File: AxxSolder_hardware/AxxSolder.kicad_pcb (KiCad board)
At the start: 2 copper layers, 39 x 71 mm, 91 parts, among them IC1 LTC4440AHMS8E-5#PBF, IC2 STM32G431KBT6, IC3 TMP236AQDBZRQ1, IC4 OPA2333AIDRBR, IC5 STM32G431KBT6, IC6 TPS54302DDCR, J1 Conn_01x07_Male, J4 Conn_01x07_Male, Q2 2N7002NXAKR, U1 PEC11L-4220F-S0015, U2 BSC014N04LS

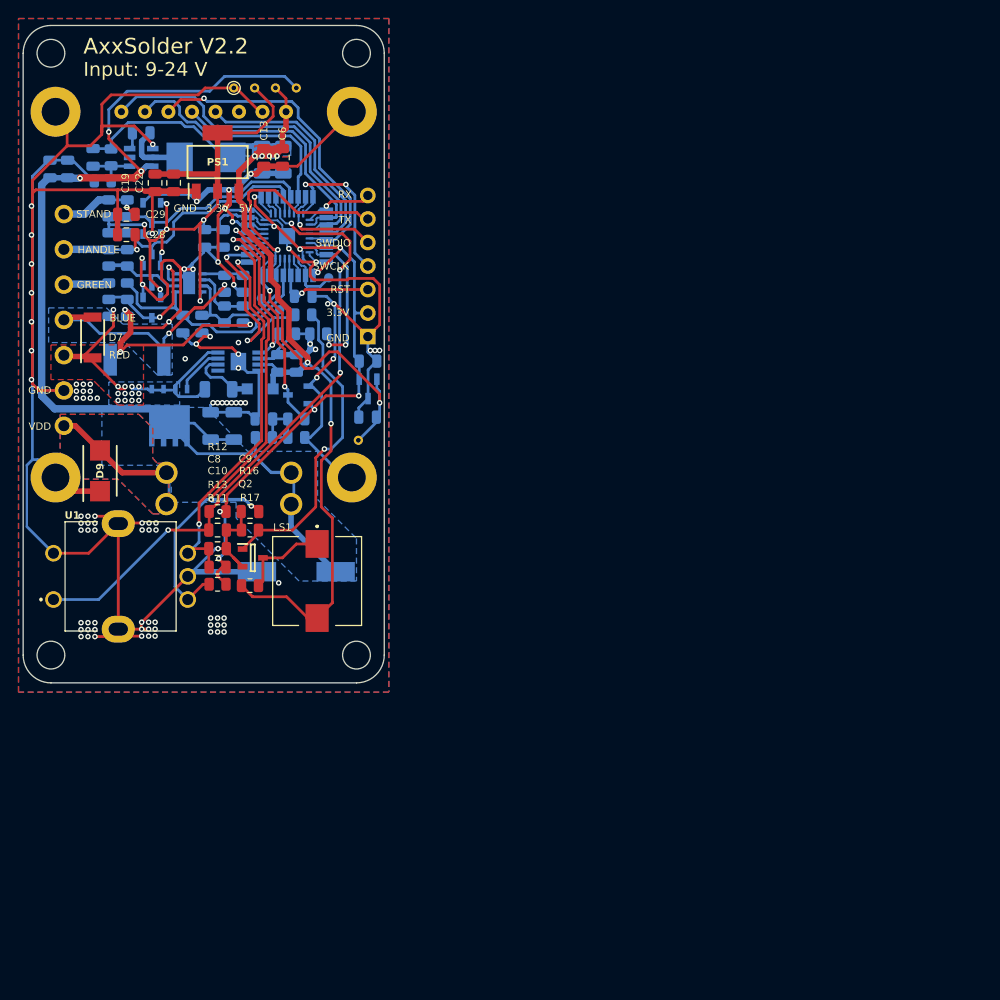
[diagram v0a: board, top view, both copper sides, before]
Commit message: update USBC-PD branch
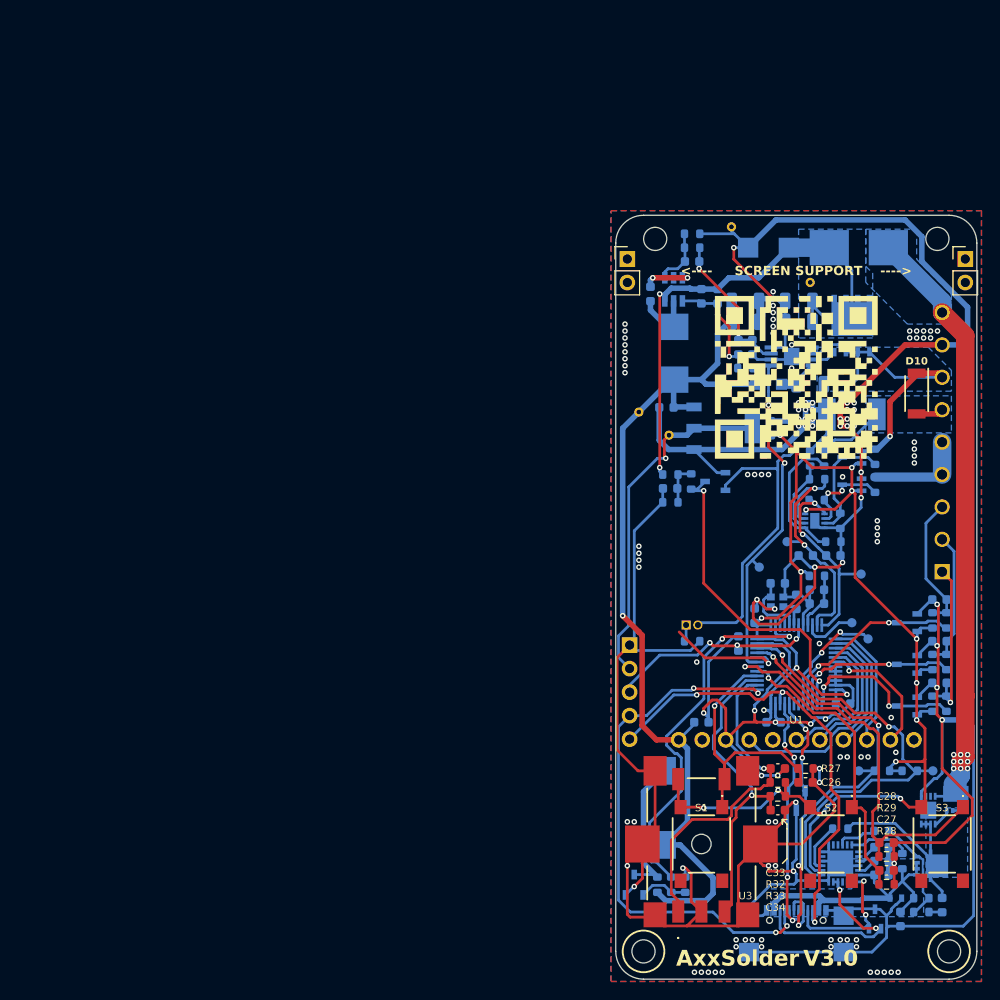
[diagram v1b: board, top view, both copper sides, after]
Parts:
- removed C23: 330u, EMZR500ARA331MJA0G:CAPAE1030X1050N
- removed the D5 at (110.9, 74.0)
- removed H3, H4: MountingHole, MountingHole:MountingHole_3mm
- removed the IC5 at (125.5, 69.8)
- removed the R16 at (121.5, 101.5)
- removed the R17 at (121.5, 107.5)
- removed the R22 at (108.2, 73.9)
- removed the R26 at (120.8, 78.2)
- removed TP3: GND_TP, TestPoint:TestPoint_THTPad_D1.0mm_Drill0.5mm
- removed U2: BSC014N04LS, BSC014N04LS:BSC014N04LS
- added C1: 100n, Capacitor_SMD:C_0603_1608Metric, B.Cu at (166.5, 88.2)
- added C17: 1u, Capacitor_SMD:C_0603_1608Metric, B.Cu at (189.7, 137.2)
- added C18: 1u, Capacitor_SMD:C_0603_1608Metric, B.Cu at (189.7, 135.8)
- added C19: 10u, Capacitor_SMD:C_0603_1608Metric, B.Cu at (191.8, 143.5)
- added C28: 100n, Capacitor_SMD:C_0603_1608Metric, F.Cu at (190.2, 135.2)
- added C29: 100n, Capacitor_SMD:C_0603_1608Metric, B.Cu at (166.9, 97.0)
- added C32: 100n, Capacitor_SMD:C_0603_1608Metric, B.Cu at (196.0, 109.0)
- added C33: 100n, Capacitor_SMD:C_0603_1608Metric, F.Cu at (178.5, 127.2)
- added C34: 100n, Capacitor_SMD:C_0603_1608Metric, F.Cu at (178.5, 131.7)
- added C4: 100n, Capacitor_SMD:C_0603_1608Metric, B.Cu at (164.8, 76.0)
- added D1: BAV199WQ-7, footprints:SOT65P210X110-3N, B.Cu at (186.5, 93.7)
- added D10: PMEG10030ELPX, footprints:SODFL4725X110N, F.Cu at (193.5, 86.8)
- added D11: ESDA25P35, footprints:ESDA25P351U1M, B.Cu at (191.2, 141.2)
- added D3: ESDA25W, footprints:SOT65P210X110-3N, B.Cu at (189.0, 143.5)
- added FB1: BLM18HE601SN1D, Resistor_SMD:R_0603_1608Metric, B.Cu at (182.7, 106.4)
- added G***: LOGO, LOGO, F.Cu at (180.5, 85.0)
- added IC1: OPA2387DSGT, footprints:SON50P200X200X80-9N, B.Cu at (182.5, 100.5)
- added J2: 691243110009, footprints:691243110009, B.Cu at (196.2, 106.0)
- added J3: Conn_01x05_Socket, Connector_PinSocket_2.54mm:PinSocket_1x05_P2.54mm_Vertical, B.Cu at (162.5, 113.9)
- added Q1: STL9P3LLH6, footprints:STL20N6F7, B.Cu at (195.0, 137.8)
- added Q3: STL10N3LLH5, footprints:STL10N3LLH5, B.Cu at (197.7, 130.4)
- added R15: 1k, Resistor_SMD:R_0603_1608Metric, B.Cu at (185.2, 133.8)
- added R18: 4k7, Resistor_SMD:R_0603_1608Metric, B.Cu at (195.2, 111.2)
- added R27: 4k7, Resistor_SMD:R_0603_1608Metric, F.Cu at (181.5, 127.2)
- added R30: 6k8, Resistor_SMD:R_0603_1608Metric, B.Cu at (166.9, 98.5)
- added R32: 4k7, Resistor_SMD:R_0603_1608Metric, F.Cu at (178.5, 128.8)
- added R33: 4k7, Resistor_SMD:R_0603_1608Metric, F.Cu at (178.5, 130.2)
- added R34: 4k7, Resistor_SMD:R_0603_1608Metric, B.Cu at (168.5, 139.8)
- added R39: 5m, footprints:RESC6432X89N, B.Cu at (186.5, 89.0)
- added R4: 4k7, Resistor_SMD:R_0603_1608Metric, B.Cu at (183.5, 93.8)
- added R40: 4k7, Resistor_SMD:R_0603_1608Metric, B.Cu at (169.2, 113.5)
- added R5: 1k5, Resistor_SMD:R_0603_1608Metric, B.Cu at (189.0, 96.6)
- added R6: 100k, Resistor_SMD:R_0603_1608Metric, B.Cu at (169.2, 71.0)
- added R7: 4k7, Resistor_SMD:R_0603_1608Metric, B.Cu at (182.0, 93.8)
- added R8: 360k, Resistor_SMD:R_0603_1608Metric, B.Cu at (182.7, 98.2)
- added R9: 220k, Resistor_SMD:R_0603_1608Metric, B.Cu at (182.8, 96.0)
- added REF**: PinHeader_1x02_P2.54mm_Vertical, Connector_PinHeader_2.54mm:PinHeader_1x02_P2.54mm_Vertical, F.Cu at (162.2, 72.2)
- added REF**: PinHeader_1x02_P2.54mm_Vertical, Connector_PinHeader_2.54mm:PinHeader_1x02_P2.54mm_Vertical, F.Cu at (198.8, 72.2)
- added S1: ADTSM644KVTR, footprints:ADTSM644KVTR, F.Cu at (170.2, 135.4)
- added S2: ADTSM644KVTR, footprints:ADTSM644KVTR, F.Cu at (184.2, 135.4)
- added S3: ADTSM644KVTR, footprints:ADTSM644KVTR, F.Cu at (196.2, 135.4)
- added TP10: DIAG_TP, TestPoint:TestPoint_Pad_D1.0mm, B.Cu at (188.2, 113.2)
- added TP11: DIAG_TP, TestPoint:TestPoint_Pad_D1.0mm, B.Cu at (187.2, 127.5)
- added TP12: DIAG_TP, TestPoint:TestPoint_Pad_D1.0mm, B.Cu at (195.2, 127.5)
- added TP4: Current_TP, TestPoint:TestPoint_Pad_D1.0mm, B.Cu at (179.5, 102.8)
- added U3: PEC11J-9220F-S0015, footprints:PEC11J9220FS0015, F.Cu at (170.2, 135.4)
- added U4: BSC014N04LS, footprints:BSC014N04LS, B.Cu at (186.5, 76.3)
- added Y1: NX2016SA-32M-EXS00A-CS06465, footprints:NX2016SA32MEXS00ACS06465, B.Cu at (178.4, 109.2)
- C10: value 100n -> 1n; footprint Capacitor_SMD:C_0805_2012Metric -> Capacitor_SMD:C_0603_1608Metric; moved to B.Cu
- C11: value 100n -> 1n; footprint Capacitor_SMD:C_0805_2012Metric -> Capacitor_SMD:C_0603_1608Metric
- C12: value 10u -> 10p; footprint Capacitor_SMD:C_0805_2012Metric -> Capacitor_SMD:C_0603_1608Metric
- C13, C22, C6: footprint Capacitor_SMD:C_0805_2012Metric -> Capacitor_SMD:C_0603_1608Metric; moved to B.Cu
- C14: value 10u -> 100n; footprint Capacitor_SMD:C_0805_2012Metric -> Capacitor_SMD:C_0603_1608Metric
- C15: value 1n -> 10u; footprint Capacitor_SMD:C_0805_2012Metric -> Capacitor_SMD:C_0603_1608Metric
- C16: value 1n -> 1u; footprint Capacitor_SMD:C_0805_2012Metric -> Capacitor_SMD:C_0603_1608Metric
- C2: renamed from C19; footprint Capacitor_SMD:C_0805_2012Metric -> Capacitor_SMD:C_0603_1608Metric; moved to B.Cu
- C20, C21, C24, C5: footprint Capacitor_SMD:C_0805_2012Metric -> Capacitor_SMD:C_0603_1608Metric
- C25: value 22u -> 10u; footprint Capacitor_SMD:C_1206_3216Metric -> Capacitor_SMD:C_0603_1608Metric
- C26: value 75p -> 100n; footprint Capacitor_SMD:C_0805_2012Metric -> Capacitor_SMD:C_0603_1608Metric; moved to F.Cu
- C27: value 22u -> 100n; footprint Capacitor_SMD:C_1206_3216Metric -> Capacitor_SMD:C_0603_1608Metric; moved to F.Cu
- C3: value 100n -> 10p; footprint Capacitor_SMD:C_0805_2012Metric -> Capacitor_SMD:C_0603_1608Metric
- C30: renamed from C29; footprint Capacitor_SMD:C_0805_2012Metric -> Capacitor_SMD:C_0603_1608Metric; moved to B.Cu
- C31: renamed from C28; footprint Capacitor_SMD:C_0805_2012Metric -> Capacitor_SMD:C_0603_1608Metric; moved to B.Cu
- C36: renamed from C1; footprint Capacitor_SMD:C_0805_2012Metric -> Capacitor_SMD:C_0603_1608Metric
- C37: renamed from C2; footprint Capacitor_SMD:C_0805_2012Metric -> Capacitor_SMD:C_0603_1608Metric
- C7: value 100n -> 75p; footprint Capacitor_SMD:C_0805_2012Metric -> Capacitor_SMD:C_0603_1608Metric
- C8, C9: value 100n -> 22u; footprint Capacitor_SMD:C_0805_2012Metric -> Capacitor_SMD:C_1206_3216Metric; moved to B.Cu
- D12: value BAT54S -> TPD2E2U06; footprint BAT54S,215:SOT95P230X110-3N -> footprints:SOT95P237X95-3N
- D2: value PMEG6020ER -> BAV199WQ-7; footprint PMEG6020ER,115:PMEG6020ER115 -> footprints:SOT65P210X110-3N
- D4: value Waveshare 1.5inch OLED Module -> SMBJ24A; footprint 1_5inch-rgb-oled-module_asm-1110:1_5inch-rgb-oled-module_asm-1110 -> footprints:DIOM5436X261N; moved to B.Cu
- D5: renamed from D6; footprint BAT54S,215:SOT95P230X110-3N -> footprints:SOT95P230X110-3N
- D6: renamed from D3; footprint BAT54S,215:SOT95P230X110-3N -> footprints:SOT95P230X110-3N
- D7: value PMEG10030ELPX -> BAT54S; footprint PMEG10030ELPX:SODFL4725X110N -> footprints:SOT95P230X110-3N; moved to B.Cu
- D8: renamed from D1; footprint BAT54S,215:SOT95P230X110-3N -> footprints:SOT95P230X110-3N
- D9: value SMBJ24CA -> PMEG6020ER; footprint SMBJ24CA:DIOM5436X261N -> footprints:PMEG6020ER115; moved to B.Cu
- F1: value 10A Fuse -> 0154007.DRL; footprint 3557-2:3557-2 -> footprints:0154100DR
- H1: footprint MountingHole:MountingHole_3mm -> MountingHole:MountingHole_2.5mm; moved to F.Cu
- H2: footprint MountingHole:MountingHole_3mm -> MountingHole:MountingHole_2.5mm
- IC2: value STM32G431KBT6 -> STM32F303CCT6TR; footprint STM32G431KBT6:QFP80P900X900X160-32N -> footprints:QFP50P900X900X160-48N
- IC3: value TMP236AQDBZRQ1 -> TPS54302DDCR; footprint TMP236AQDBZRQ1:SOT95P237X112-3N -> footprints:SOT95P280X110-6N
- IC4: value OPA2333AIDRBR -> STUSB4500QTR; footprint OPA2333AIDRBR:SON65P300X300X100-9N-D -> footprints:QFN50P400X400X100-25N-D
- IC5: renamed from IC1; value LTC4440AHMS8E-5#PBF -> LTC4440AHMS8E; footprint LTC4440AHMS8E-5#PBF:SOP65P490X110-9N -> footprints:SOP65P490X110-9N
- IC6: value TPS54302DDCR -> MAX16171ATA_VY+T; footprint TPS54302DDCR:SOT95P280X110-6N -> footprints:SON50P300X200X80-9N
- J1: value Conn_01x07_Male -> USB4110-GF-A; footprint 691243310007:691243310007 -> footprints:USB4110GFA
- J4: value Conn_01x07_Male -> Conn_01x02_Pin; footprint Connector_PinSocket_2.54mm:PinSocket_1x07_P2.54mm_Vertical -> Connector_PinHeader_1.27mm:PinHeader_1x02_P1.27mm_Vertical
- L1: value SRP7028CC-100M -> SRP7028CC; footprint SRP7028CC-100M:INDPM7366X300N -> footprints:INDPM7366X300N
- LS1: footprint CMI-9653S-SMT-TR:CMI9653SSMTTR -> footprints:CMI9653SSMTTR; moved to B.Cu
- PS1: footprint LD1117AS33TR:SOT230P700X190-4N -> footprints:SOT230P700X190-4N; moved to B.Cu
- Q2: footprint 2N7002NXAKR:SOT95P230X110-3N -> footprints:SOT95P230X110-3N; moved to B.Cu
- R1: value 4k7 -> 1k5; footprint Resistor_SMD:R_0805_2012Metric -> Resistor_SMD:R_0603_1608Metric
- R10: value 2m -> 13k3; footprint WSLP25122L500FEA:RESC6432X89N -> Resistor_SMD:R_0603_1608Metric
- R11: value 10k -> 22k; footprint Resistor_SMD:R_0805_2012Metric -> Resistor_SMD:R_0603_1608Metric; moved to B.Cu
- R12: value 10k -> 100; footprint Resistor_SMD:R_0805_2012Metric -> Resistor_SMD:R_0603_1608Metric; moved to B.Cu
- R13: value 10k -> 1k; footprint Resistor_SMD:R_0805_2012Metric -> Resistor_SMD:R_0603_1608Metric; moved to B.Cu
- R14: value 10k -> 22k; footprint Resistor_SMD:R_0805_2012Metric -> Resistor_SMD:R_0603_1608Metric
- R16: renamed from R8; value 10k -> 4k7; footprint Resistor_SMD:R_0805_2012Metric -> Resistor_SMD:R_0603_1608Metric
- R17: renamed from R9; value 10k -> 4k7; footprint Resistor_SMD:R_0805_2012Metric -> Resistor_SMD:R_0603_1608Metric
- R19, R20: value 1k5 -> 4k7; footprint Resistor_SMD:R_0805_2012Metric -> Resistor_SMD:R_0603_1608Metric
- R2: value 47k -> 360k; footprint Resistor_SMD:R_0805_2012Metric -> Resistor_SMD:R_0603_1608Metric
- R21: value 470k -> 47k; footprint Resistor_SMD:R_0805_2012Metric -> Resistor_SMD:R_0603_1608Metric
- R22: renamed from R6; footprint Resistor_SMD:R_0805_2012Metric -> Resistor_SMD:R_0603_1608Metric
- R23, R24: value 220k -> 4k7; footprint Resistor_SMD:R_0805_2012Metric -> Resistor_SMD:R_0603_1608Metric
- R25: footprint Resistor_SMD:R_0805_2012Metric -> Resistor_SMD:R_0603_1608Metric
- R26: renamed from R5; footprint Resistor_SMD:R_0805_2012Metric -> Resistor_SMD:R_0603_1608Metric
- R28: value 100k -> 4k7; footprint Resistor_SMD:R_0805_2012Metric -> Resistor_SMD:R_0603_1608Metric; moved to F.Cu
- R29: value 13k3 -> 4k7; footprint Resistor_SMD:R_0805_2012Metric -> Resistor_SMD:R_0603_1608Metric; moved to F.Cu
- R3: value 6k8 -> 220k; footprint Resistor_SMD:R_0805_2012Metric -> Resistor_SMD:R_0603_1608Metric
- R31: renamed from R15; footprint Resistor_SMD:R_0805_2012Metric -> Resistor_SMD:R_0603_1608Metric
- R35: renamed from R18; value 10k -> 4k7; footprint Resistor_SMD:R_0805_2012Metric -> Resistor_SMD:R_0603_1608Metric
- TP1: value AmbTemp_TP -> VDD_TP
- TP2: value TestPoint -> 3.3V_TP; footprint TestPoint:TestPoint_Pad_D1.0mm -> TestPoint:TestPoint_THTPad_D1.0mm_Drill0.5mm
- TP5: value Thermocouple_TP -> TC_TP
- TP6: value Current_TP -> GND_TP; footprint TestPoint:TestPoint_Pad_D1.0mm -> TestPoint:TestPoint_THTPad_D1.0mm_Drill0.5mm
- TP7: value 5V_TP -> VDD_TP
- TP8: value VDD_TP -> SW_TP; footprint TestPoint:TestPoint_THTPad_D1.0mm_Drill0.5mm -> TestPoint:TestPoint_Pad_D1.0mm
- TP9: value 3.3V_TP -> DIAG_TP; footprint TestPoint:TestPoint_THTPad_D1.0mm_Drill0.5mm -> TestPoint:TestPoint_Pad_D1.0mm
- U1: value PEC11L-4220F-S0015 -> ~; footprint PEC11L-4220F-S0015:PEC11L4220FS0015 -> footprints:Adafruit_240x320_TFT
- moved R28 114.8 mm to (190.2, 139.8), turned to 0 degrees
- moved R29 111.7 mm to (190.2, 136.8), turned to 0 degrees
- moved IC6 110.4 mm to (194.8, 131.8), turned to 90 degrees
- moved C13 109.0 mm to (196.2, 142.0)
- moved J1 104.0 mm to (180.5, 146.2), turned to 180 degrees
- moved R16 103.8 mm to (195.2, 120.2)
- moved R26 103.4 mm to (196.7, 120.2)
- moved C26 102.4 mm to (181.5, 128.8), turned to 0 degrees
- moved H2 102.1 mm to (197.0, 147.0)
- moved C21 101.7 mm to (185.6, 120.2), turned to 0 degrees
- moved C30 101.3 mm to (196.0, 118.0)
- moved C27 100.7 mm to (190.2, 138.2), turned to 0 degrees
- moved R17 99.9 mm to (195.2, 115.8), turned to 90 degrees
- moved R22 99.5 mm to (196.7, 115.8), turned to 90 degrees
- moved C31 98.2 mm to (196.0, 113.5)
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- renumbered C4 to C35, C17 to C38, C18 to C39
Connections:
- C10 pad 1: /ENC_A -> /TC
- C11 pad 1: +3.3V -> /Current
- C12 pad 1: +3.3V -> GND
- C12 pad 2: GND -> Net-(IC2-PF1/OSC_OUT)
- C13 pad 1: GND -> Net-(C13-Pad1)
- C13 pad 2: +5V -> /VDD_IN_USBCPD
- C14 pad 2: VDD -> /NRST
- C15 pad 1: /Thermocouple -> GND
- C15 pad 2: GND -> +5V
- C16 pad 1: /Current -> /VBUS
- C20 pad 1: /Ambient_temp -> +3.3V
- C21 pad 1: GND -> +3.3V
- C21 pad 2: VDD -> GND
- C24 pad 1: Net-(IC6-BOOT) -> /VCCA
- C24 pad 2: Net-(IC6-SW) -> GND
- C25 pad 1: GND -> /VCCA
- C25 pad 2: +5V -> GND
- C26 pad 1: Net-(IC6-FB) -> /SW1
- C26 pad 2: +5V -> GND
- C27 pad 1: GND -> /SW2
- C27 pad 2: +5V -> GND
- C3 pad 1: Net-(C3-Pad1) -> Net-(IC2-PF0/OSC_IN)
- C31 pad 1: /Handle_sense -> /Handle_sense2
- C35 pad 2: Net-(IC1-BOOST) -> Net-(IC5-TS)
- C5 pad 1: +3.3V -> GND
- C5 pad 2: GND -> VDD
- C6 pad 2: +5V -> VDD
- C7 pad 1: GND -> Net-(IC3-FB)
- C7 pad 2: /NRST -> +5V
- C8 pad 1: /ENC_Button -> GND
- C8 pad 2: GND -> +5V
- C9 pad 1: /ENC_B -> GND
- C9 pad 2: GND -> +5V
- D12 pad 1: GND -> /USB_D+
- D12 pad 2: +3.3V -> /USB_D-
- D12 pad 3: /Busvoltage -> GND
- D2 pad 1: Net-(IC1-BOOST) -> GND
- D2 pad 2: +5V -> +3.3V
- D4 pad 1: +5V -> VDD
- D5 pad 3: Net-(D6-common) -> /Handle_inp1
- D6 pad 3: /Handle_inp -> /Handle_inp2
- D7 pad 1: /RED -> GND
- D7 pad 2: /BLUE -> +3.3V
- D9 pad 1: GND -> Net-(IC5-TS)
- D9 pad 2: Net-(J1-Pin_7) -> +5V
- F1 pad 2: Net-(J1-Pin_7) -> /VDD_IN
- IC2 pad 10: /Buzzer -> /USR1
- IC2 pad 11: /ENC_B -> /Current
- IC2 pad 12: /Heater -> /TC
- IC2 pad 13: /Busvoltage -> /SPI_DC
- IC2 pad 14: GND -> /SPI_RST
- IC2 pad 15: +3.3V -> /SPI_SCK
- IC2 pad 16: GND -> /SPI_CS
- IC2 pad 17: +3.3V -> /SPI_MOSI
- IC2 pad 18: Net-(IC2-PA8) -> /SD_CS
- IC2 pad 19: /ENC_Button -> GND
- IC2 pad 2: Net-(IC2-PF0-OSC_IN) -> /Buzzer
- IC2 pad 20: /Handle_inp -> GND
- IC2 pad 21: /Stand_inp -> GND
- IC2 pad 22: /SPI_DC -> GND
- IC2 pad 23: /SWDIO -> GND
- IC2 pad 24: /SWCLK -> +3.3V
- IC2 pad 25: /MCU_RX -> /Stand_inp
- IC2 pad 26: /SPI_SCK -> /VDD_inp
- IC2 pad 27: /SPI_RST -> /Handle_inp2
- IC2 pad 28: /SPI_MOSI -> /Handle_inp1
- IC2 pad 29: /SPI_CS -> /USR2
- IC2 pad 3: Net-(IC2-PF1-OSC_OUT) -> unconnected-(IC2-PC14/OSC32_IN-Pad3)
- IC2 pad 30: Net-(IC2-PB7) -> unconnected-(IC2-PA9-Pad30)
- IC2 pad 31: Net-(IC2-PB8-BOOT0) -> unconnected-(IC2-PA10-Pad31)
- IC2 pad 32: GND -> /USB_D-
- IC2 pad 4: /NRST -> unconnected-(IC2-PC15/OSC32_OUT-Pad4)
- IC2 pad 5: /Thermocouple -> Net-(IC2-PF0/OSC_IN)
- IC2 pad 6: /Current -> Net-(IC2-PF1/OSC_OUT)
- IC2 pad 7: /MCU_TX -> /NRST
- IC2 pad 8: /Ambient_temp -> GND
- IC2 pad 9: /ENC_A -> /VCCA
- IC3 pad 1: +3.3V -> GND
- IC3 pad 2: /Ambient_temp -> Net-(IC3-SW)
- IC3 pad 3: GND -> VDD
- IC4 pad 1: /Thermocouple -> /CC1
- IC4 pad 2: Net-(D5-common) -> /CC1
- IC4 pad 3: Net-(D6-common) -> (no net)
- IC4 pad 4: GND -> /CC2
- IC4 pad 5: Net-(IC4-+IN_B) -> /CC2
- IC4 pad 6: Net-(IC4--IN_B) -> GND
- IC4 pad 7: /Current -> /SCL
- IC4 pad 8: +3.3V -> /SDA
- IC4 pad 9: GND -> Net-(IC4-DISCH)
- IC5 pad 6: Net-(IC1-BOOST) -> /RED
- IC5 pad 8: /RED -> Net-(IC5-TS)
- IC6 pad 1: GND -> Net-(IC6-GATE)
- IC6 pad 2: Net-(IC6-SW) -> /VDD_IN_USBCPD
- IC6 pad 3: VDD -> /VDD_IN_USBCPD
- IC6 pad 4: Net-(IC6-FB) -> /VDD_IN_USBCPD
- IC6 pad 5: unconnected-(IC6-EN-Pad5) -> GND
- IC6 pad 6: Net-(IC6-BOOT) -> (no net)
- J4 pad 1: GND -> /BOOT0
- L1 pad 1: Net-(IC6-SW) -> Net-(IC3-SW)
- R1 pad 1: Net-(C3-Pad1) -> /RED
- R1 pad 2: /Busvoltage -> Net-(IC1A-+)
- R10 pad 1: /BLUE -> Net-(IC3-FB)
- R11 pad 1: /ENC_B -> Net-(Q1-G)
- R11 pad 2: +3.3V -> /VBUS
- R12 pad 1: +3.3V -> Net-(Q1-G)
- R12 pad 2: /ENC_Button -> Net-(C13-Pad1)
- R13 pad 1: +3.3V -> /VBUS
- R13 pad 2: /ENC_A -> Net-(IC4-VBUS_VS_DISCH)
- R14 pad 1: GND -> Net-(IC4-VBUS_EN_SNK)
- R14 pad 2: Net-(IC2-PB8-BOOT0) -> Net-(Q1-G)
- R17 pad 2: /Handle_sense -> /Handle_sense2
- R19 pad 1: /GREEN -> /Handle_inp1
- R19 pad 2: Net-(D5-common) -> /Handle_sense1
- R2 pad 1: VDD -> Net-(IC1A-+)
- R2 pad 2: Net-(C3-Pad1) -> GND
- R20 pad 1: /RED -> +5V
- R20 pad 2: Net-(D6-common) -> Net-(LS1--)
- R21 pad 1: Net-(D6-common) -> VDD
- R21 pad 2: GND -> Net-(C29-Pad1)
- R22 pad 1: /Handle_inp -> /Handle_inp2
- R22 pad 2: /Handle_sense -> /Handle_sense2
- R23 pad 1: Net-(IC4-+IN_B) -> /SCL
- R23 pad 2: GND -> +3.3V
- R24 pad 1: Net-(IC4--IN_B) -> /SDA
- R24 pad 2: /Current -> +3.3V
- R25 pad 1: Net-(IC4-+IN_B) -> Net-(C29-Pad1)
- R25 pad 2: /BLUE -> /VDD_inp
- R28 pad 1: +5V -> /SW2
- R28 pad 2: Net-(IC6-FB) -> GND
- R29 pad 1: Net-(IC6-FB) -> /SW3
- R3 pad 1: Net-(C3-Pad1) -> Net-(IC1B-+)
- TP1 pad 1: /Ambient_temp -> +5V
- TP2 pad 1: Net-(IC2-PF0-OSC_IN) -> +3.3V
- TP5 pad 1: /Thermocouple -> /TC
- TP6 pad 1: /Current -> GND
- TP7 pad 1: +5V -> VDD
- TP8 pad 1: VDD -> /Heater
- TP9 pad 1: +3.3V -> /USR1
- U1 pad 1: /ENC_Button -> +5V
- U1 pad 2: GND -> unconnected-(U1-NC-Pad2)
- U1 pad 3: /ENC_B -> GND
- U1 pad 4: GND -> /SPI_SCK
- U1 pad 5: /ENC_A -> unconnected-(U1-NC-Pad5)
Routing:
- net GND: track 451.4 -> 600.5 mm, vias 103 -> 132
- net +3.3V: track 153.7 -> 231.8 mm, vias 16 -> 19
- net /ENC_Button: track 69.0 -> 0.00 mm, vias 4 -> 0
- net VDD: track 122.6 -> 56.9 mm, vias 3 -> 2
- net /VDD_IN: track 0.00 -> 64.2 mm, vias 0 -> 9
- net /SDA: track 0.00 -> 46.8 mm, vias 0 -> 2
- net /SW3: track 0.00 -> 43.2 mm, vias 0 -> 1
- net /SCL: track 0.00 -> 40.5 mm, vias 0 -> 2
- net /SWCLK: track 18.3 -> 57.9 mm, vias 2 -> 4
- net /SWDIO: track 11.8 -> 50.7 mm, vias 1 -> 3
- net /VDD_inp: track 0.00 -> 34.8 mm, vias 0 -> 2
- net /Ambient_temp: track 33.6 -> 0.00 mm, vias 2 -> 0
- net /SW2: track 0.00 -> 31.8 mm, vias 0 -> 1
- net /VBUS: track 0.00 -> 31.6 mm
- net /Thermocouple: track 30.8 -> 0.00 mm
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- added copper zone on B.Cu, net /VBUS
- added copper zone on B.Cu, net /VDD_IN
- added copper zone on B.Cu, net /VDD_IN_USBCPD
- removed copper zone on B.Cu, net +5V
- removed copper zone on F.Cu, net +5V
- removed copper zone on F.Cu, net /RED
- removed copper zone on B.Cu, net Net-(J1-Pin_7)
- removed copper zone on F.Cu, net Net-(J1-Pin_7)
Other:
- board size 39 x 71 mm -> 39 x 82.5 mm
- board text added: "2025-01"
- board text added: "9-24 V"
- board text added: "<---- SCREEN SUPPORT ---->"
- board text added: "AxxSolder"
- board text added: "BLU"
- board text added: "BOOT0"
- board text added: "GRN"
- board text added: "IN1"
- board text added: "IN2"
- board text added: "Input Voltage"
- board text added: "SCL"
- board text added: "SDA"
- board text added: "STND"
- board text added: "STUSB4500"
- board text added: "SW"
- board text added: "USBC-PD 100W"
- board text added: "USR1"
- board text added: "USR2"
- board text added: "V3.0"
- board text added: "V_IN"
- board text removed: "+"
- board text removed: "-"
- board text removed: "AxxSolder V2.2"
- board text removed: "BLUE"
- board text removed: "CLK"
- board text removed: "DIO"
- board text removed: "GREEN"
- board text removed: "HANDLE"
- board text removed: "Input: 9-24 V"
- board text removed: "RST"
- board text removed: "RX"
- board text removed: "STAND"
- board text removed: "SWD"
- board text removed: "TMP"
- board text removed: "TX"
- board text removed: "VDD+"

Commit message: update and migrate to new MCU work
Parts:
- R30: value 6k8 -> 4k7
- R31: value 220 -> 100
- moved TP6 59.6 mm to (195.7, 124.1)
- moved IC6 1.00 mm to (193.8, 131.7)
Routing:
- net /VDD_IN: track 64.2 -> 65.2 mm
- net Net-(IC6-GATE): track 2.07 -> 3.04 mm
- net GND: track 600.5 -> 601.3 mm
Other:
- board text added: "V3.1"

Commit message: updates in hardware and software
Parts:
- removed C12, C3: 10p, Capacitor_SMD:C_0603_1608Metric
- removed C15: 10u, Capacitor_SMD:C_0603_1608Metric
- removed D10: PMEG10030ELPX, footprints:SODFL4725X110N
- removed IC2: STM32F303CCT6TR, footprints:QFP50P900X900X160-48N
- removed J4: Conn_01x02_Pin, Connector_PinHeader_1.27mm:PinHeader_1x02_P1.27mm_Vertical
- removed R40: 4k7, Resistor_SMD:R_0603_1608Metric
- removed Y1: NX2016SA-32M-EXS00A-CS06465, footprints:NX2016SA32MEXS00ACS06465
- added D13: PMEG6020ER, footprints:PMEG6020ER115, B.Cu at (188.2, 85.8)
- added IC7: STM32G431CBT6, footprints:QFP50P900X900X160-48N, B.Cu at (181.1, 111.9)
- added R41: 22k, Resistor_SMD:R_0603_1608Metric, B.Cu at (166.9, 94.0)
- added TP13: DIAG_TP, TestPoint:TestPoint_Pad_D1.0mm, B.Cu at (170.0, 120.5)
- added TP14: TC_TP, TestPoint:TestPoint_Pad_D1.0mm, B.Cu at (177.6, 100.0)
- added TP15: DIAG_TP, TestPoint:TestPoint_Pad_D1.0mm, B.Cu at (189.2, 106.4)
- C16, C17, C18: value 1u -> 10u
- C26, C27, C28, C33, C34, R27, R28, R29, R32, R33: moved to B.Cu
- R10: value 13k3 -> 22k
- R13, R15: value 1k -> 1k5
- R21: value 47k -> 22k
- R6: value 100k -> 220k
- TP1: value VDD_TP -> DIAG_TP; footprint TestPoint:TestPoint_THTPad_D1.0mm_Drill0.5mm -> TestPoint:TestPoint_Pad_D1.0mm
- TP6: footprint TestPoint:TestPoint_THTPad_D1.0mm_Drill0.5mm -> TestPoint:TestPoint_THTPad_D2.0mm_Drill1.0mm
- moved TP1 30.2 mm to (170.0, 118.2)
- moved TP10 18.5 mm to (170.0, 116.0)
- moved TP9 16.7 mm to (170.0, 113.8)
- moved C27 13.6 mm to (179.8, 129.6), turned to 180 degrees
- moved C28 13.6 mm to (179.8, 126.6), turned to 180 degrees
- moved R28 13.6 mm to (179.8, 131.1), turned to 180 degrees
- moved R29 13.6 mm to (179.8, 128.1), turned to 180 degrees
- moved FB1 11.2 mm to (188.5, 116.0), turned to 0 degrees
- moved TP8 9.00 mm to (178.8, 96.8)
- moved R27 8.83 mm to (173.7, 131.3)
- moved C25 8.78 mm to (188.5, 114.5), turned to 0 degrees
- moved C14 8.70 mm to (178.0, 105.9), turned to 180 degrees
- moved C26 7.92 mm to (173.7, 129.8)
- moved C33 7.37 mm to (173.7, 132.8), turned to 180 degrees
- moved R32 7.37 mm to (173.7, 134.3), turned to 180 degrees
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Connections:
- net /Current renamed /CURRENT
- net /VDD_inp renamed /VBUS_IN
- C1 pad 2: +5V -> +6V
- C36 pad 1: +5V -> +6V
- C37 pad 1: +5V -> +6V
- C7 pad 2: +5V -> +6V
- C8 pad 2: +5V -> +6V
- C9 pad 2: +5V -> +6V
- D9 pad 2: +5V -> +6V
- IC5 pad 3: +5V -> +6V
- J1 pad A8: /SWCLK -> /SWDIO
- J1 pad B8: /SWDIO -> /SWCLK
- L1 pad 2: +5V -> +6V
- LS1 pad 2: +5V -> +6V
- PS1 pad 3: +5V -> +6V
- R20 pad 1: +5V -> +6V
- R21 pad 1: VDD -> Net-(R21-Pad1)
- R6 pad 1: +5V -> +6V
- TP1 pad 1: +5V -> /USR3
- U1 pad 2: unconnected-(U1-NC-Pad2) -> +3.3V
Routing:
- net +5V: track 123.6 -> 0.00 mm, vias 3 -> 0
- net +6V: track 0.00 -> 117.5 mm, vias 0 -> 4
- net GND: track 601.3 -> 504.8 mm, vias 132 -> 137
- net +3.3V: track 231.8 -> 197.4 mm, vias 19 -> 14
- net /USR4: track 0.00 -> 31.3 mm, vias 0 -> 2
- net /USR3: track 0.00 -> 28.8 mm, vias 0 -> 2
- net /USART_TX: track 0.00 -> 19.0 mm, vias 0 -> 1
- net /USR1: track 5.90 -> 23.1 mm, vias 0 -> 2
- net /VBUS_IN: track 34.8 -> 19.0 mm
- net /USB_D-: track 30.2 -> 45.0 mm, vias 4 -> 2
- net /BOOT0: track 14.6 -> 0.00 mm, vias 1 -> 0
- net /USR2: track 12.7 -> 26.0 mm
- net /Heater: track 38.7 -> 27.3 mm
- net /CURRENT: track 28.4 -> 17.2 mm, vias 2 -> 3
- net /SPI_SCK: track 24.8 -> 14.3 mm, vias 0 -> 1
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- added copper zone on B.Cu, net +3.3V
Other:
- board text added: "IO1"
- board text added: "IO2"
- board text added: "IO3"
- board text added: "IO4"
- board text added: "USBC-PD"
- board text removed: "5V"
- board text removed: "BOOT0"
- board text removed: "USBC-PD 100W"
- board text removed: "USR1"
- board text removed: "USR2"
- board text removed: "V3.1"
